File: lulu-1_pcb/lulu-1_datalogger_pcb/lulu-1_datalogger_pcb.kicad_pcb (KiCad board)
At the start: 2 copper layers, 38 parts, among them J1 B2B-XH-A, J2 SBH11-PBPC-D10-ST-BK, J3 MEM2067-02-180-00-A_REVB, SW1 SW_Nidec_CAS-120A1, U1 STM32F401RETx, U2 BAT54LT1G, U3 LP3982ILD-3.3, U4 BMP280, U5 MPU-6050, U6 W25Q16JVSS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

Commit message: something
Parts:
- added BZ1: Buzzer, AT_1224_TWT_5V_2_R:XDCR_AT-1224-TWT-5V-2-R, F.Cu at (264.0, 74.8)
- added D1: LED, 151031VS06000:WL-TMRC_3MM, F.Cu at (247.3, 68.5)
- added D2: LED, 151031VS06000:WL-TMRC_3MM, F.Cu at (247.3, 77.6)
- added D3: LED, 151031VS06000:WL-TMRC_3MM, F.Cu at (247.5, 85.0)
- added D4: LED, 151031VS06000:WL-TMRC_3MM, F.Cu at (201.2, 47.0)
- added R10: 100Ω, Resistor_SMD:R_0805_2012Metric_Pad1.20x1.40mm_HandSolder, F.Cu at (253.5, 85.0)
- added R11: 100Ω, Resistor_SMD:R_0805_2012Metric_Pad1.20x1.40mm_HandSolder, F.Cu at (206.7, 47.0)
- added R7: 100Ω, Resistor_SMD:R_0805_2012Metric_Pad1.20x1.40mm_HandSolder, F.Cu at (253.0, 66.0)
- added R8: 100Ω, Resistor_SMD:R_0805_2012Metric_Pad1.20x1.40mm_HandSolder, F.Cu at (253.5, 77.5)
- moved C17 6.04 mm to (182.5, 64.3)
- moved C19 6.04 mm to (182.5, 70.3)
- moved C15 6.04 mm to (182.5, 58.3)
- moved C16 6.04 mm to (182.5, 61.3)
- moved C10 6.04 mm to (178.0, 64.3)
- moved C12 6.04 mm to (178.0, 70.3)
- moved C13 6.04 mm to (178.0, 73.3)
- moved C3 6.04 mm to (173.6, 64.3)
- moved C5 6.04 mm to (173.6, 70.3)
- moved C6 6.04 mm to (173.6, 73.3)
- moved R4 6.04 mm to (186.9, 67.1)
- moved R5 6.04 mm to (186.9, 70.0)
- moved R6 6.04 mm to (186.9, 73.0)
- moved C18 6.04 mm to (182.5, 67.3)
- moved C1 6.04 mm to (173.6, 58.3)
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- renumbered R7 to R9
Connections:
- U1 pad 10: unconnected-(U1-PC2-Pad10) -> LED1
- U1 pad 11: unconnected-(U1-PC3-Pad11) -> LED2
- U1 pad 24: unconnected-(U1-PC4-Pad24) -> LED3
- U1 pad 25: unconnected-(U1-PC5-Pad25) -> BUZZ
- U1 pad 44: PA11 -> unconnected-(U1-PA11-Pad44)
- U1 pad 45: PA12 -> unconnected-(U1-PA12-Pad45)

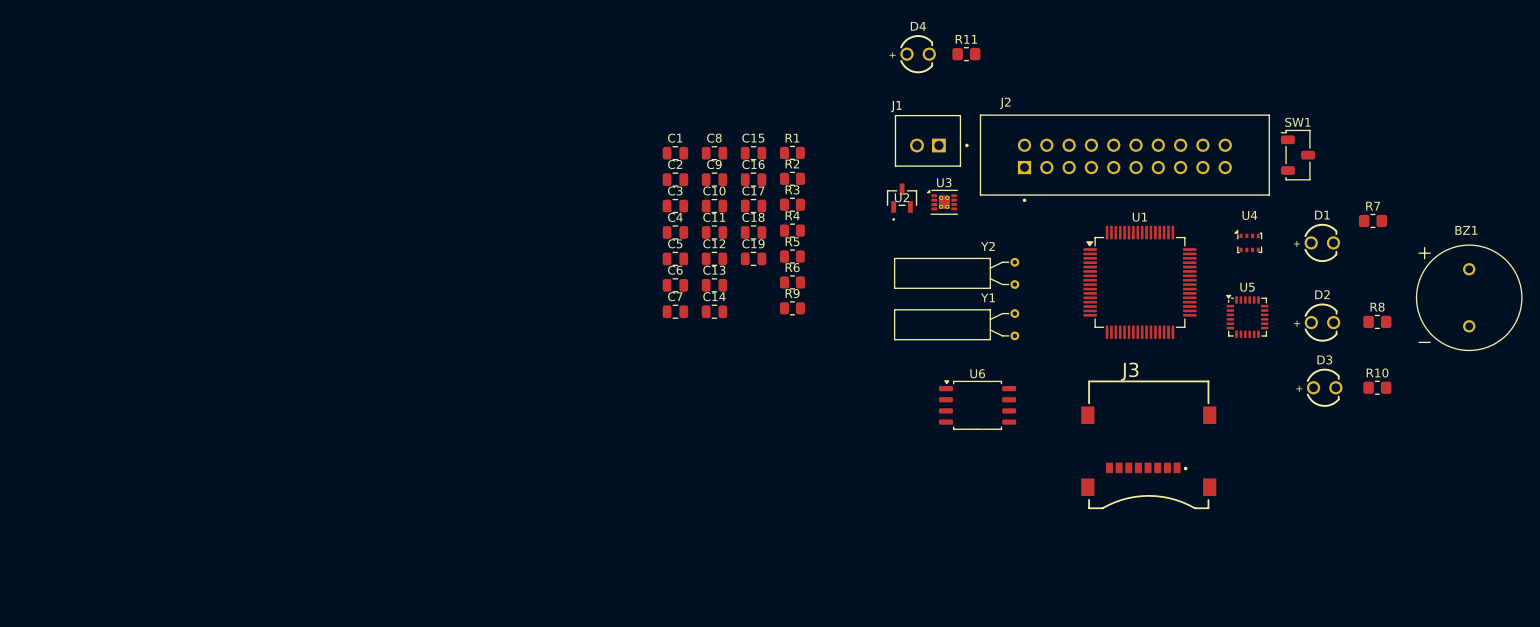
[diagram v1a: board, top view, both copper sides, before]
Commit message: fixed LED polarity on schematic
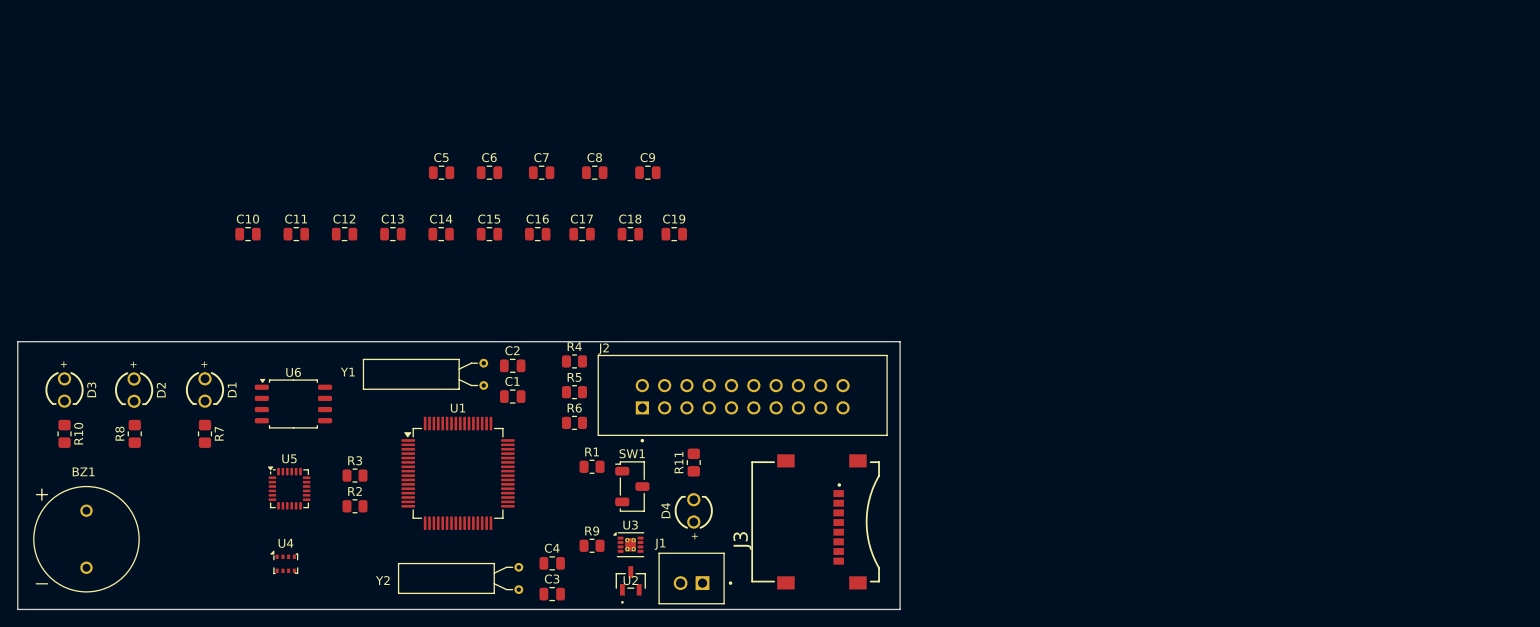
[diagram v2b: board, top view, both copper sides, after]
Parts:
- moved BZ1 159.9 mm to (106.5, 102.2)
- moved R10 149.6 mm to (104.0, 90.2), turned to -90 degrees
- moved D3 143.5 mm to (104.0, 85.2), turned to -90 degrees
- moved R8 142.1 mm to (112.0, 90.2), turned to 90 degrees
- moved D2 135.6 mm to (111.9, 85.3), turned to -90 degrees
- moved R7 135.2 mm to (120.0, 90.2), turned to -90 degrees
- moved D1 128.4 mm to (120.0, 85.2), turned to -90 degrees
- moved U4 115.7 mm to (129.2, 105.0)
- moved U5 110.9 mm to (129.6, 96.5)
- moved SW1 84.7 mm to (168.7, 96.2)
- moved U1 80.7 mm to (148.8, 94.8)
- moved U6 77.9 mm to (130.1, 86.8)
- moved Y2 66.3 mm to (155.8, 105.5)
- moved R2 62.2 mm to (137.1, 98.5)
- moved Y1 60.8 mm to (151.8, 82.2)
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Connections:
- D1 pad 1: LED3 -> Net-(D1-K)
- D1 pad 2: Net-(D1-A) -> LED3
- D2 pad 1: LED2 -> Net-(D2-K)
- D2 pad 2: Net-(D2-A) -> LED2
- D3 pad 1: LED1 -> Net-(D3-K)
- D3 pad 2: Net-(D3-A) -> LED1
- R10 pad 2: Net-(D3-A) -> Net-(D3-K)
- R7 pad 2: Net-(D1-A) -> Net-(D1-K)
- R8 pad 2: Net-(D2-A) -> Net-(D2-K)
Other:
- board outline added: 100.5 x 30.5 mm

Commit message: initial pcb layout
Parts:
- moved C19 55.5 mm to (128.4, 100.0), turned to 90 degrees
- moved C17 52.7 mm to (127.5, 106.5), turned to -90 degrees
- moved C15 51.0 mm to (119.5, 106.5), turned to -90 degrees
- moved C16 50.0 mm to (120.0, 100.0), turned to 90 degrees
- moved C18 49.1 mm to (128.5, 96.0), turned to 90 degrees
- moved C12 46.4 mm to (168.0, 101.0)
- moved C10 46.2 mm to (155.1, 102.5)
- moved C11 44.4 mm to (164.1, 96.5)
- moved C13 43.8 mm to (164.1, 105.0)
- moved C9 41.9 mm to (155.1, 99.5)
- moved C6 41.1 mm to (159.6, 101.0)
- moved C14 39.3 mm to (119.9, 96.1), turned to 90 degrees
- moved C8 37.2 mm to (155.1, 96.5)
- moved C7 33.2 mm to (155.1, 93.5)
- moved C5 30.6 mm to (155.0, 90.0)
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
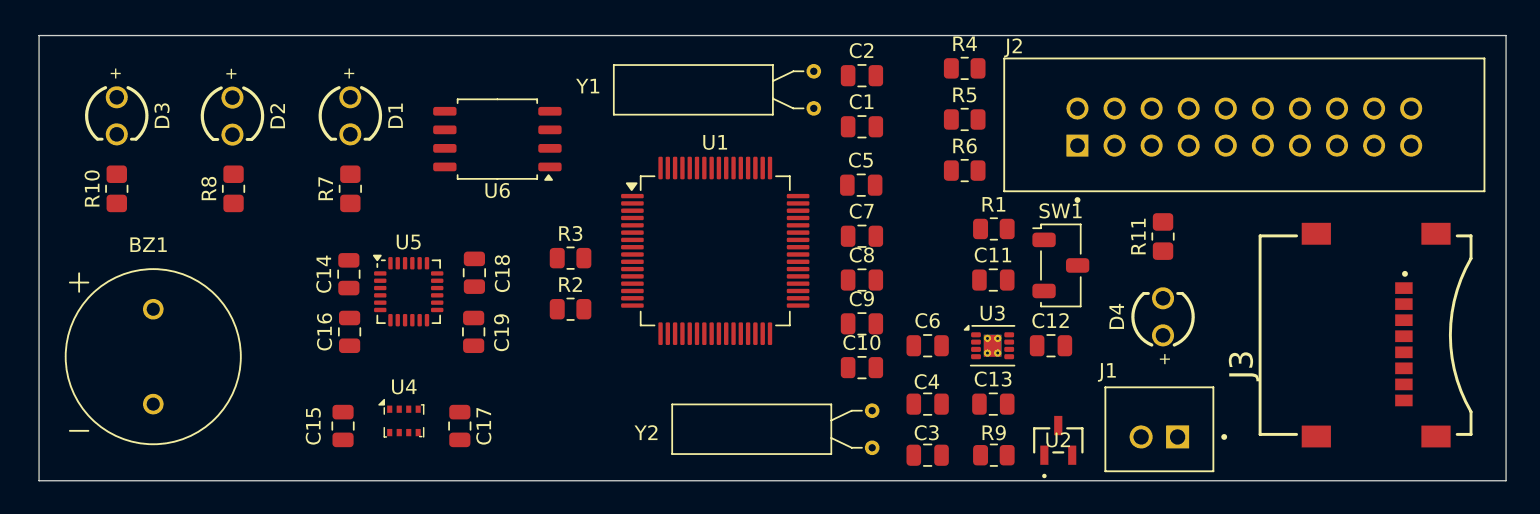
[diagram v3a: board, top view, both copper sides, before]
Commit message: added mounting holes
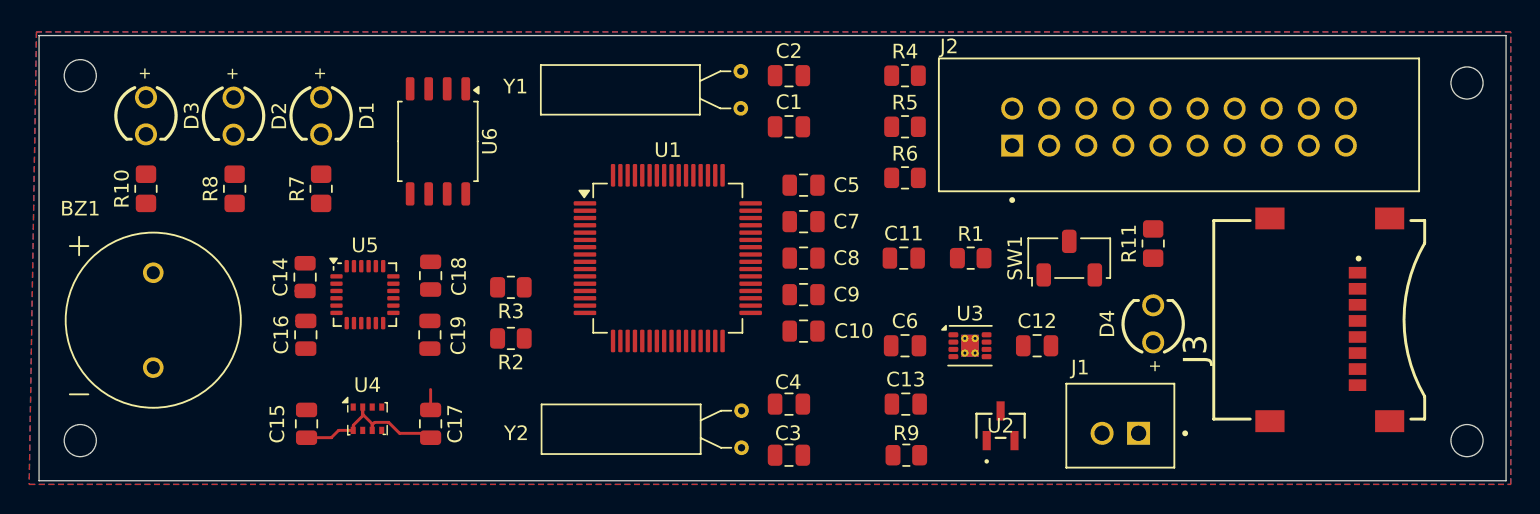
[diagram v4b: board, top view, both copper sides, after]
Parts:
- added REF**: MountingHole_2.2mm_M2, MountingHole:MountingHole_2.2mm_M2, F.Cu at (196.5, 83.0)
- added REF**: MountingHole_2.2mm_M2, MountingHole:MountingHole_2.2mm_M2, F.Cu at (101.5, 107.5)
- added REF**: MountingHole_2.2mm_M2, MountingHole:MountingHole_2.2mm_M2, F.Cu at (101.5, 82.5)
- added REF**: MountingHole_2.2mm_M2, MountingHole:MountingHole_2.2mm_M2, F.Cu at (196.5, 107.5)
- moved C3 9.50 mm to (150.1, 108.5)
- moved C4 9.50 mm to (150.1, 105.0)
- moved Y2 8.95 mm to (146.8, 105.5)
- moved C11 6.32 mm to (157.9, 95.0)
- moved C13 6.00 mm to (158.1, 105.0)
- moved R9 6.00 mm to (158.1, 108.5)
- moved C1 5.00 mm to (150.1, 86.0)
- moved C2 5.00 mm to (150.1, 82.5)
- moved Y1 5.00 mm to (146.8, 82.2)
- moved C10 4.72 mm to (151.1, 100.0)
- moved R2 4.55 mm to (131.0, 100.5), turned to 180 degrees
- moved R3 4.55 mm to (131.0, 97.0), turned to 180 degrees
- moved J2 4.47 mm to (176.8, 86.0)
- moved C9 4.47 mm to (151.1, 97.5)
- moved C8 4.27 mm to (151.1, 95.0)
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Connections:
- U4 pad 2: VDD -> +3V3
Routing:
- net +3V3: track 0.00 -> 12.0 mm
- net GND: track 0.00 -> 2.95 mm
- added copper zone on B.Cu, net GND
- added copper zone on F.Cu, net GND

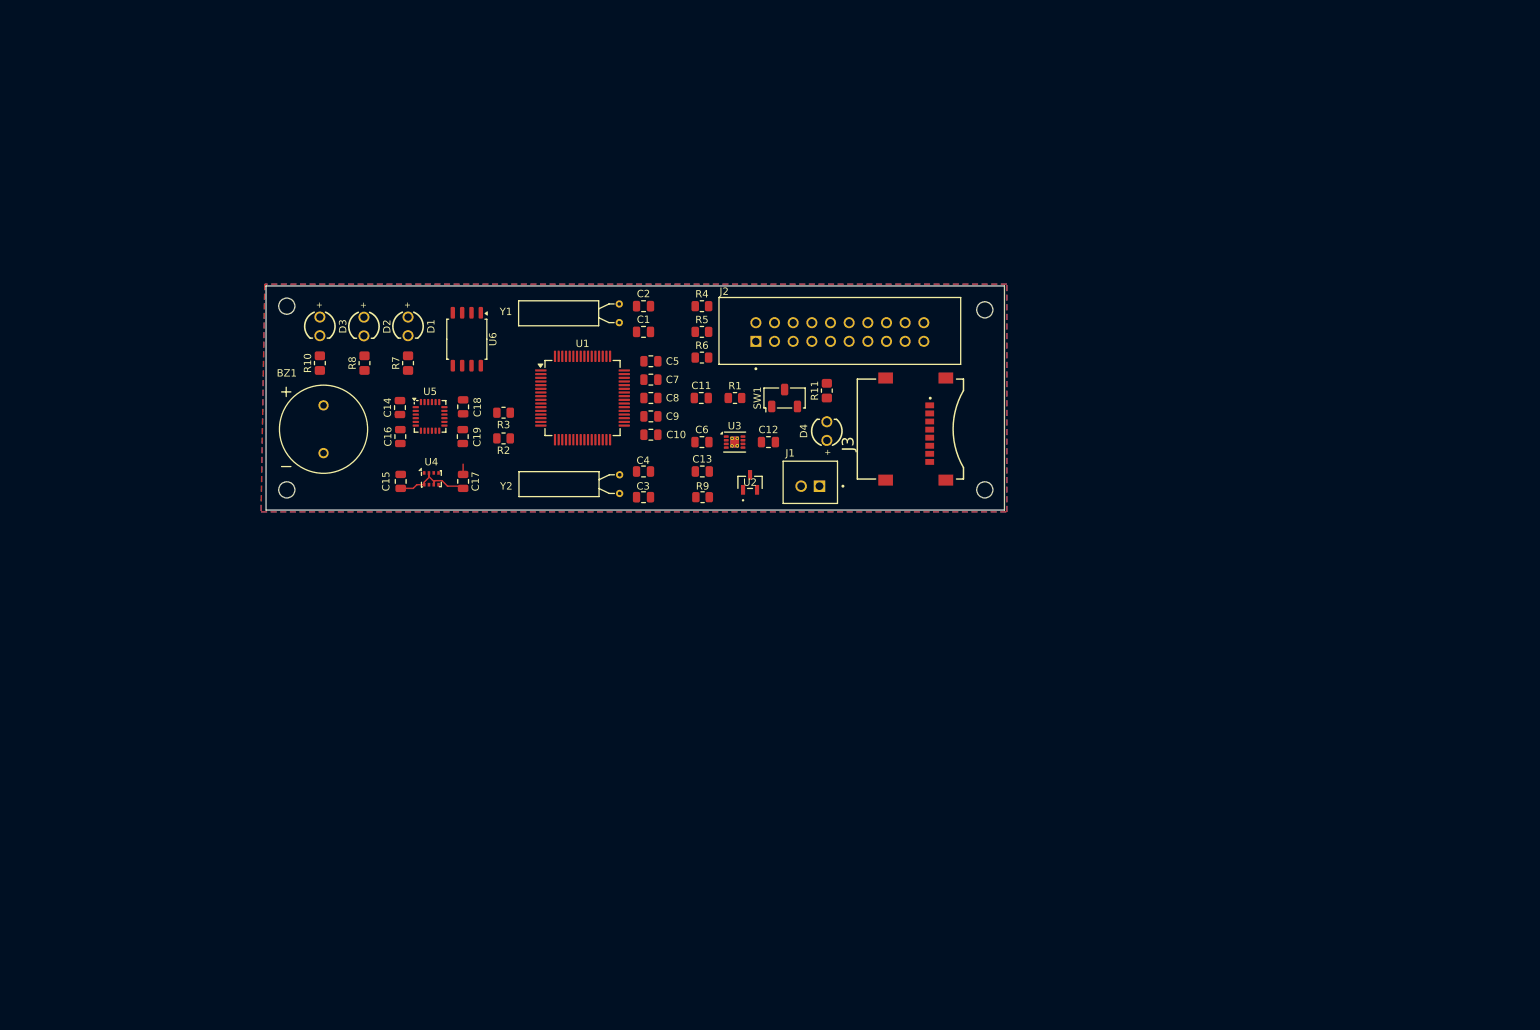
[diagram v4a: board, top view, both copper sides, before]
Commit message: finished initial traces. however errors in DRC to be resolved
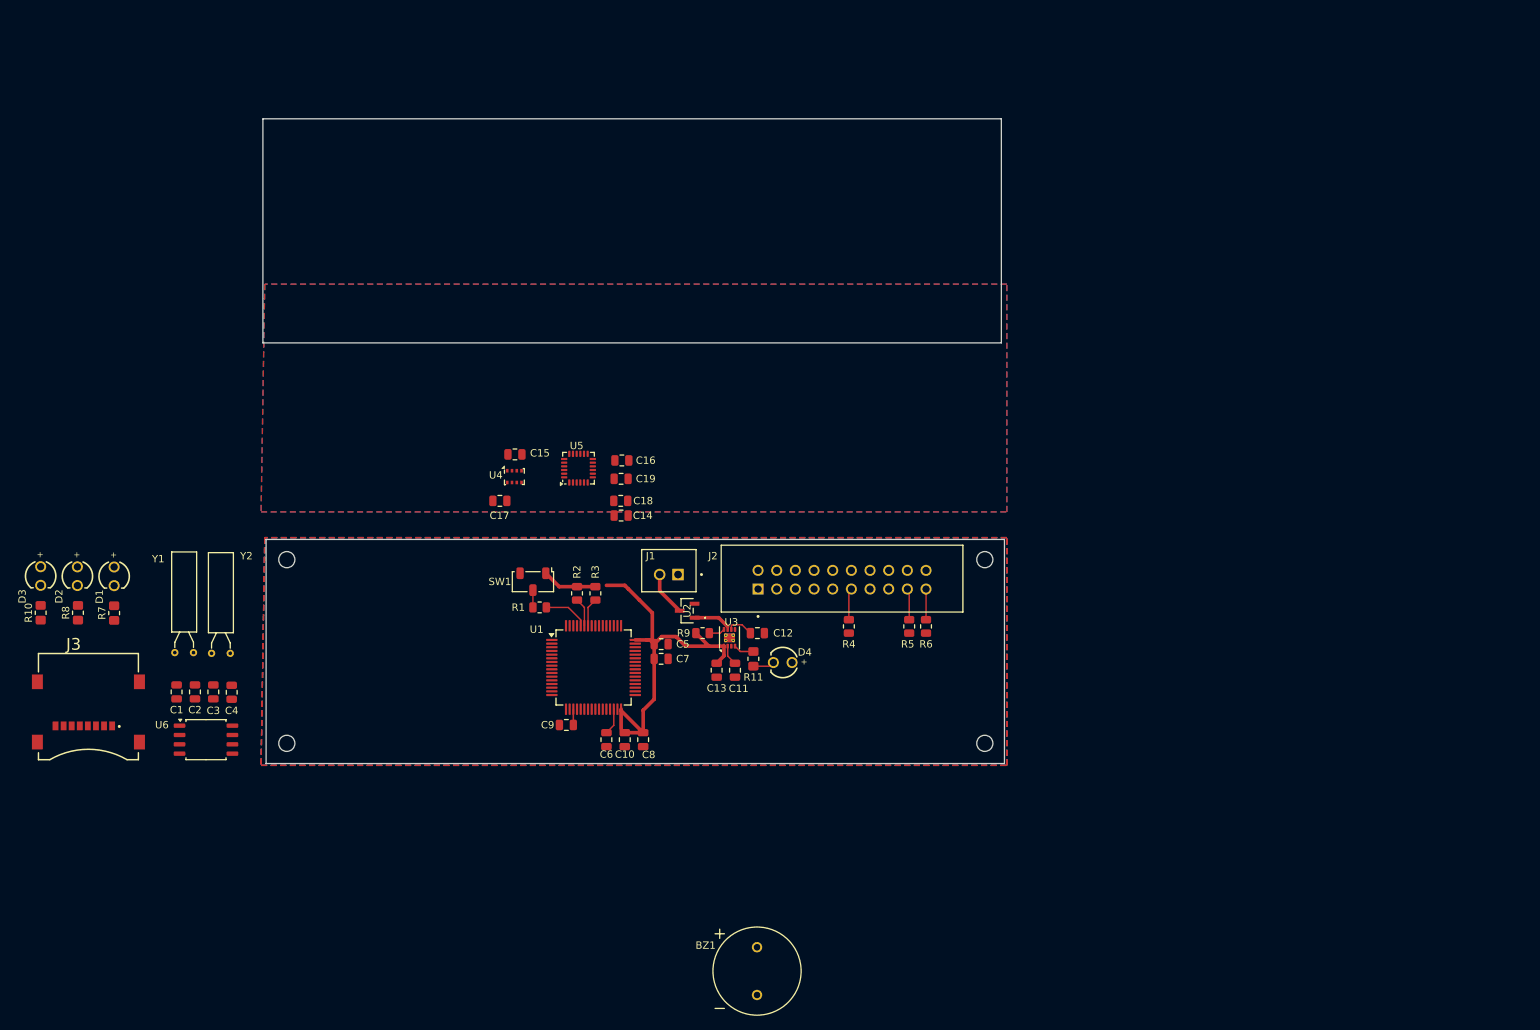
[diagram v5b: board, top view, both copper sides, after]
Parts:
- moved J3 118.1 mm to (74.5, 137.0), turned to 0 degrees
- moved BZ1 94.4 mm to (165.5, 173.0)
- moved C2 80.5 mm to (89.0, 135.0), turned to 90 degrees
- moved C1 80.2 mm to (86.5, 135.0), turned to 90 degrees
- moved Y1 74.9 mm to (88.8, 129.7), turned to 180 degrees
- moved U6 65.0 mm to (90.5, 141.5), turned to 0 degrees
- moved C3 64.3 mm to (91.5, 135.0), turned to 90 degrees
- moved C4 63.6 mm to (94.0, 135.1), turned to 90 degrees
- moved Y2 58.3 mm to (93.8, 129.8), turned to 180 degrees
- moved D1 52.5 mm to (78.0, 119.3)
- moved R7 52.5 mm to (78.0, 124.3)
- moved D2 51.7 mm to (73.0, 119.2)
- moved R8 51.7 mm to (73.1, 124.2)
- moved D3 51.0 mm to (68.0, 119.2)
- moved R10 51.0 mm to (68.0, 124.2)
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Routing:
- net +3V3: track 12.0 -> 58.7 mm
- net VBUS: track 0.00 -> 14.2 mm
- net +3.3V: track 0.00 -> 7.51 mm
- net Net-(U1-BOOT0): track 0.00 -> 6.18 mm
- net Net-(J2-Pad11): track 0.00 -> 4.32 mm
- net Net-(J2-Pad17): track 0.00 -> 4.28 mm
- net Net-(J2-Pad19): track 0.00 -> 4.17 mm
- net PB7: track 0.00 -> 3.91 mm
- net PB6: track 0.00 -> 3.91 mm
- net Net-(U3-CC): track 0.00 -> 3.63 mm
- net Net-(U1-VCAP1): track 0.00 -> 3.61 mm
- net GND: track 2.95 -> 0.00 mm
- net Net-(D4-A): track 0.00 -> 2.94 mm
- net Net-(SW1-B): track 0.00 -> 2.35 mm
- net Net-(U3-~{FAULT}): track 0.00 -> 2.21 mm
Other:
- board size 100.5 x 30.5 mm -> 100.9 x 87.8 mm
